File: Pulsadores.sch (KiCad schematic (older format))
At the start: 8 parts

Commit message: version preliminar de la etapa de alimentacion
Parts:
- removed R? (x4): 10K, Resistencias:R_0805, symbol R
- removed SW? (x3): Pulsador_2p, symbol Pulsador_2p
- added P10, P6, P7, P8, P9: CONN_01X01, Conectores:Pad_Conector_Cocodrilo, symbol CONN_01X01
- added R39, R40, R41, R42: 10K, Resistencias:R_0805, symbol R
- added R43, R44, R45, R46: 10M, Resistencias:R_0805, symbol R
- added SW1, SW3, SW4: Pulsador_2p, symbol Pulsador_2p
- gave numbers to parts that had none: 1
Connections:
- net labels added: +5V, A0, A1, A2, A3, PB0, PB1, PB2, PB3
- net labels removed: +3V3
- wire segments 24 -> 40
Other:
- moved on the sheet: SW2

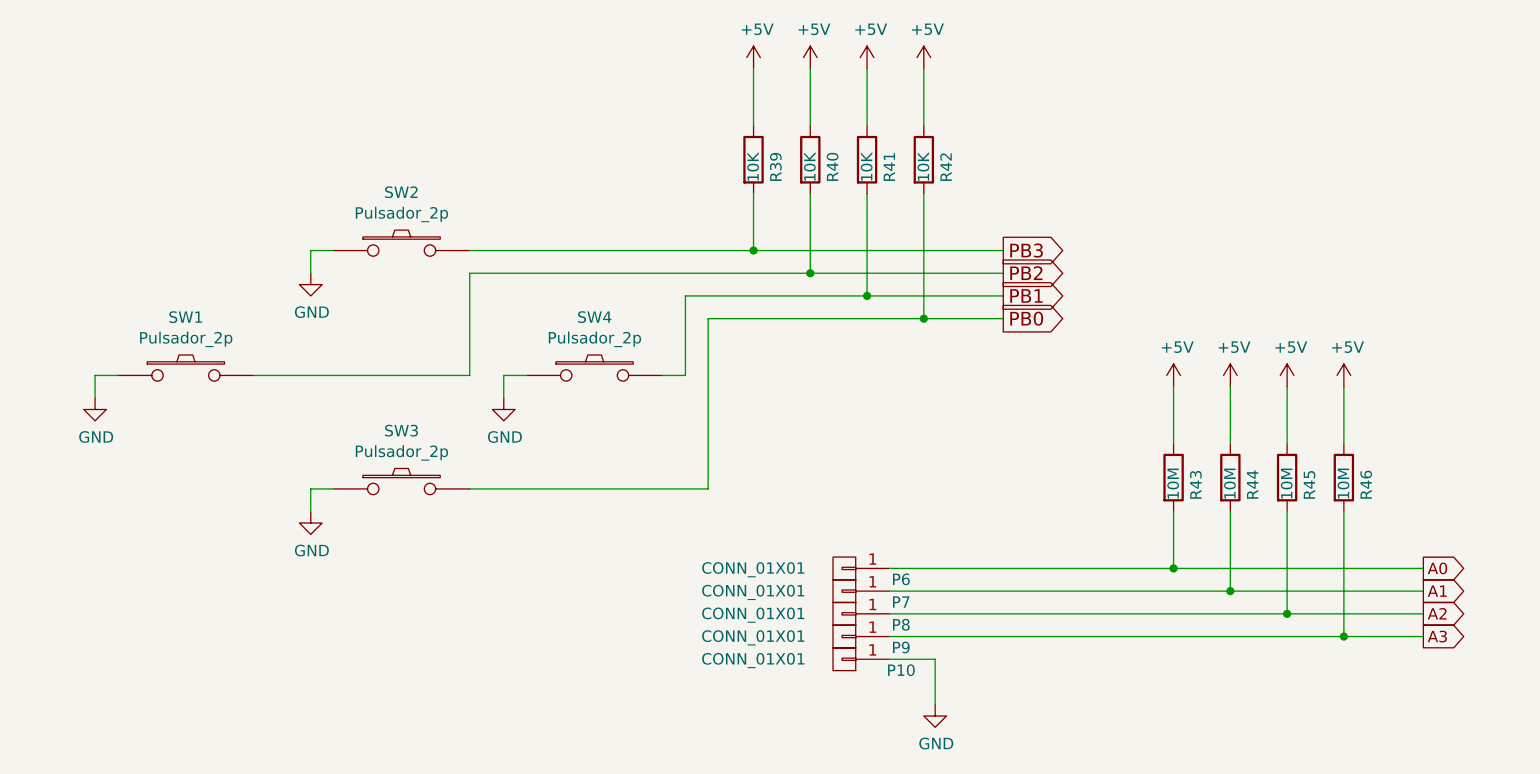
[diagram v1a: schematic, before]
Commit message: asignacion inicial de huellas
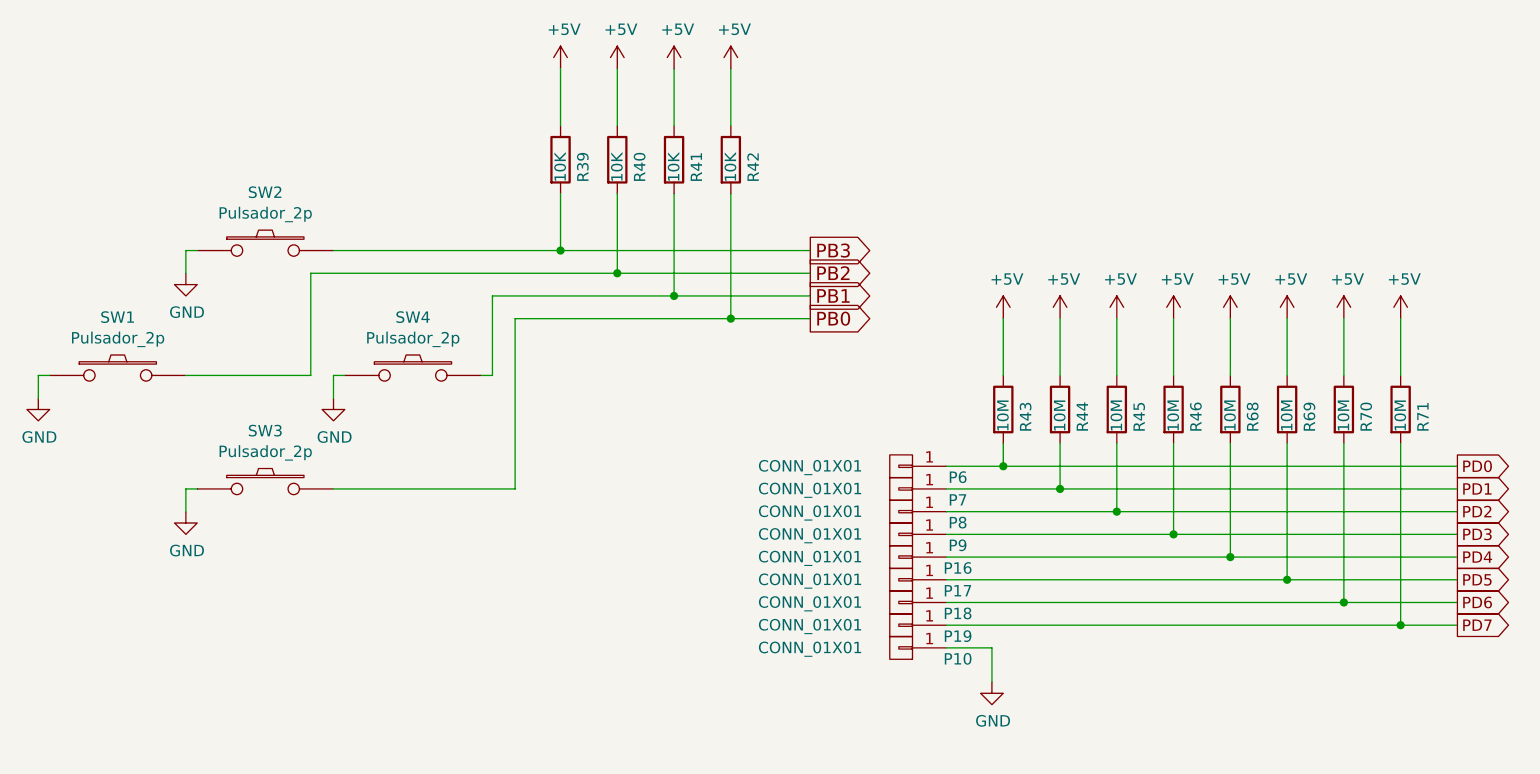
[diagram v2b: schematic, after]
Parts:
- added P16, P17, P18, P19: CONN_01X01, Conectores:Pad_Conector_Cocodrilo, symbol CONN_01X01
- added R68, R69, R70, R71: 10M, Resistencias:R_0805, symbol R
- SW1, SW2, SW3, SW4: footprint (none) -> Relays_and_Contacts:CANAL_ELECTRONIC_DTSM-31N-B
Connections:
- net +5V: now also R68.1, R69.1, R70.1, R71.1
- net A0 renamed PD0
- net A1 renamed PD1
- net A2 renamed PD2
- net A3 renamed PD3
- new net PD4: P16.1 (P1), R68.2
- new net PD5: P17.1 (P1), R69.2
- new net PD6: P18.1 (P1), R70.2
- new net PD7: P19.1 (P1), R71.2
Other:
- moved on the sheet: P10, P6, P7, P8, P9, R39, R40, R41, R42, R43, R44, R45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

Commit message: cambiar ch340T por ch340g y añadir nc a pines
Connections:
- net PB0 renamed PB4
- net PB1 renamed PB5
- net PB2 renamed PB6
- net PB3 renamed PB7
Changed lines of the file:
@@
 $Descr User 8268 5846
 encoding utf-8
-Sheet 10 15
+Sheet 10 14
 Title "Bloque de pulsadores"
 Date "2017-01-25"
@@
 	800  2300 800  2400
 $Comp
-L GND #PWR086
+L GND #PWR094
 U 1 1 588EA502
 P 800 2400
-F 0 "#PWR086" H 800 2150 50  0001 C CNN
+F 0 "#PWR094" H 800 2150 50  0001 C CNN
 F 1 "GND" H 805 2227 50  0000 C CNN
 F 2 "" H 800 2400 50  0000 C CNN
@@
 	1450 2800 1450 2900
 $Comp
-L GND #PWR087
+L GND #PWR095
 U 1 1 588EA503
 P 1450 2900
-F 0 "#PWR087" H 1450 2650 50  0001 C CNN
+F 0 "#PWR095" H 1450 2650 50  0001 C CNN
 F 1 "GND" H 1455 2727 50  0000 C CNN
 F 2 "" H 1450 2900 50  0000 C CNN
@@
 	1450 1750 1450 1850
 $Comp
-L GND #PWR088
+L GND #PWR096
 U 1 1 588EA504
 P 1450 1850
-F 0 "#PWR088" H 1450 1600 50  0001 C CNN
+F 0 "#PWR096" H 1450 1600 50  0001 C CNN
 F 1 "GND" H 1455 1677 50  0000 C CNN
 F 2 "" H 1450 1850 50  0000 C CNN
@@
 	2100 2300 2100 2400
 $Comp
-L GND #PWR089
+L GND #PWR097
 U 1 1 588EA505
 P 2100 2400
-F 0 "#PWR089" H 2100 2150 50  0001 C CNN
+F 0 "#PWR097" H 2100 2150 50  0001 C CNN
 F 1 "GND" H 2105 2227 50  0000 C CNN
 F 2 "" H 2100 2400 50  0000 C CNN
@@
 	3100 1200 3100 950
 $Comp
-L +5V #PWR090
+L +5V #PWR098
 U 1 1 588EA50A
 P 3100 950
-F 0 "#PWR090" H 3100 800 50  0001 C CNN
+F 0 "#PWR098" H 3100 800 50  0001 C CNN
 F 1 "+5V" H 3115 1123 50  0000 C CNN
 F 2 "" H 3100 950 50  0000 C CNN
@@
 $EndComp
 $Comp
-L +5V #PWR091
+L +5V #PWR099
 U 1 1 588EA50B
 P 3350 950
-F 0 "#PWR091" H 3350 800 50  0001 C CNN
+F 0 "#PWR099" H 3350 800 50  0001 C CNN
 F 1 "+5V" H 3365 1123 50  0000 C CNN
 F 2 "" H 3350 950 50  0000 C CNN
@@
 $EndComp
 $Comp
-L +5V #PWR092
+L +5V #PWR0100
 U 1 1 588EA50C
 P 3600 950
-F 0 "#PWR092" H 3600 800 50  0001 C CNN
+F 0 "#PWR0100" H 3600 800 50  0001 C CNN
 F 1 "+5V" H 3615 1123 50  0000 C CNN
 F 2 "" H 3600 950 50  0000 C CNN
@@
 $EndComp
 $Comp
-L +5V #PWR093
+L +5V #PWR0101
 U 1 1 588EA50D
 P 3850 950
-F 0 "#PWR093" H 3850 800 50  0001 C CNN
+F 0 "#PWR0101" H 3850 800 50  0001 C CNN
 F 1 "+5V" H 3865 1123 50  0000 C CNN
 F 2 "" H 3850 950 50  0000 C CNN
@@
 $EndBitmap
 Text GLabel 4200 2050 2    60   Output ~ 0
-PB0
+PB4
 Text GLabel 4200 1950 2    60   Output ~ 0
-PB1
+PB5
 Text GLabel 4200 1850 2    60   Output ~ 0
-PB2
+PB6
 Text GLabel 4200 1750 2    60   Output ~ 0
-PB3
+PB7
 $Comp
 L R R43
@@
 	5050 2300 5050 2050
 $Comp
-L +5V #PWR094
+L +5V #PWR0102
 U 1 1 588EA512
 P 5050 2050
-F 0 "#PWR094" H 5050 1900 50  0001 C CNN
+F 0 "#PWR0102" H 5050 1900 50  0001 C CNN
 F 1 "+5V" H 5065 2223 50  0000 C CNN
 F 2 "" H 5050 2050 50  0000 C CNN
@@
 $EndComp
 $Comp
-L +5V #PWR095
+L +5V #PWR0103
 U 1 1 588EA513
 P 5300 2050
-F 0 "#PWR095" H 5300 1900 50  0001 C CNN
+F 0 "#PWR0103" H 5300 1900 50  0001 C CNN
 F 1 "+5V" H 5315 2223 50  0000 C CNN
 F 2 "" H 5300 2050 50  0000 C CNN
@@
 $EndComp
 $Comp
-L +5V #PWR096
+L +5V #PWR0104
 U 1 1 588EA514
 P 5550 2050
-F 0 "#PWR096" H 5550 1900 50  0001 C CNN
+F 0 "#PWR0104" H 5550 1900 50  0001 C CNN
 F 1 "+5V" H 5565 2223 50  0000 C CNN
 F 2 "" H 5550 2050 50  0000 C CNN
@@
 $EndComp
 $Comp
-L +5V #PWR097
+L +5V #PWR0105
 U 1 1 588EA515
 P 5800 2050
-F 0 "#PWR097" H 5800 1900 50  0001 C CNN
+F 0 "#PWR0105" H 5800 1900 50  0001 C CNN
 F 1 "+5V" H 5815 2223 50  0000 C CNN
 F 2 "" H 5800 2050 50  0000 C CNN
@@
 $EndComp
 $Comp
-L GND #PWR098
+L GND #PWR0106
 U 1 1 588EA51B
 P 5000 3650
-F 0 "#PWR098" H 5000 3400 50  0001 C CNN
+F 0 "#PWR0106" H 5000 3400 50  0001 C CNN
 F 1 "GND" H 5005 3477 50  0000 C CNN
 F 2 "" H 5000 3650 50  0000 C CNN
@@
 	6050 2300 6050 2050
 $Comp
-L +5V #PWR099
+L +5V #PWR0107
 U 1 1 589139C8
 P 6050 2050
-F 0 "#PWR099" H 6050 1900 50  0001 C CNN
+F 0 "#PWR0107" H 6050 1900 50  0001 C CNN
 F 1 "+5V" H 6065 2223 50  0000 C CNN
 F 2 "" H 6050 2050 50  0000 C CNN
@@
 $EndComp
 $Comp
-L +5V #PWR0100
+L +5V #PWR0108
 U 1 1 589139CE
 P 6300 2050
-F 0 "#PWR0100" H 6300 1900 50  0001 C CNN
+F 0 "#PWR0108" H 6300 1900 50  0001 C CNN
 F 1 "+5V" H 6315 2223 50  0000 C CNN
 F 2 "" H 6300 2050 50  0000 C CNN
@@
 $EndComp
 $Comp
-L +5V #PWR0101
+L +5V #PWR0109
 U 1 1 589139D4
 P 6550 2050
-F 0 "#PWR0101" H 6550 1900 50  0001 C CNN
+F 0 "#PWR0109" H 6550 1900 50  0001 C CNN
 F 1 "+5V" H 6565 2223 50  0000 C CNN
 F 2 "" H 6550 2050 50  0000 C CNN
@@
 $EndComp
 $Comp
-L +5V #PWR0102
+L +5V #PWR0110
 U 1 1 589139DA
 P 6800 2050
-F 0 "#PWR0102" H 6800 1900 50  0001 C CNN
+F 0 "#PWR0110" H 6800 1900 50  0001 C CNN
 F 1 "+5V" H 6815 2223 50  0000 C CNN
 F 2 "" H 6800 2050 50  0000 C CNN
